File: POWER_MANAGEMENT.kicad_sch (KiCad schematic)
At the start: 13 parts, among them J5 LIPO PIN

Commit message: Revision
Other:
- moved on the sheet: NCD0603G1, R7
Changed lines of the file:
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@@
+	(wire
+		(pts
+			(xy 40.64 81.28) (xy 40.64 85.09)
+		)
+		(stroke
+			(width 0)
+			(type default)
+		)
+	)
 	(wire
 		(pts
@@
 	(wire
 		(pts
-			(xy 49.53 93.98) (xy 49.53 101.6)
+			(xy 40.64 90.17) (xy 40.64 97.79)
 		)
 		(stroke
@@
 	(wire
 		(pts
-			(xy 49.53 116.84) (xy 49.53 109.22)
+			(xy 40.64 114.3) (xy 40.64 105.41)
 		)
 		(stroke
@@
 	(hierarchical_label "LED"
 		(shape input)
-		(at 49.53 88.9 90)
+		(at 40.64 81.28 90)
 		(effects
 			(font
@@
 	(symbol
 		(lib_id "Device:R_Small")
-		(at 49.53 91.44 0)
+		(at 40.64 87.63 0)
 		(unit 1)
 		(exclude_from_sim no)
@@
 		(dnp no)
 		(property "Reference" "R7"
-			(at 54.61 91.44 0)
+			(at 45.72 87.63 0)
 			(effects
 				(font
@@
 		)
 		(property "Value" "5.4k"
-			(at 55.372 87.884 0)
+			(at 46.482 84.074 0)
 			(effects
 				(font
@@
 		)
 		(property "Footprint" "Resistor_SMD:R_0402_1005Metric"
-			(at 49.53 91.44 0)
+			(at 40.64 87.63 0)
 			(effects
 				(font
@@
 		)
 		(property "Datasheet" "~"
-			(at 49.53 91.44 0)
+			(at 40.64 87.63 0)
 			(effects
 				(font
@@
 		)
 		(property "Description" "Resistor, small symbol"
-			(at 49.53 91.44 0)
+			(at 40.64 87.63 0)
 			(effects
 				(font
@@
 		)
 		(property "SNAPEDA_PN" ""
-			(at 49.53 91.44 0)
+			(at 40.64 87.63 0)
 			(effects
 				(font
@@
 		(dnp no)
 		(property "Reference" "NCD0603R1"
-			(at 73.9775 102.87 90)
+			(at 75.946 101.854 90)
 			(effects
 				(font
@@
 		)
 		(property "Value" "RED_LED"
-			(at 73.9775 105.41 90)
+			(at 75.946 104.394 90)
 			(effects
 				(font
@@
 	(symbol
 		(lib_id "power:GND")
-		(at 49.53 116.84 0)
+		(at 40.64 114.3 0)
 		(unit 1)
 		(exclude_from_sim no)
@@
 		(dnp no)
 		(property "Reference" "#PWR035"
-			(at 49.53 123.19 0)
+			(at 40.64 120.65 0)
 			(effects
 				(font
@@
 		)
 		(property "Value" "GND"
-			(at 56.134 120.142 0)
+			(at 47.244 117.602 0)
 			(effects
 				(font
@@
 		)
 		(property "Footprint" ""
-			(at 49.53 116.84 0)
+			(at 40.64 114.3 0)
 			(effects
 				(font
@@
 		)
 		(property "Datasheet" ""
-			(at 49.53 116.84 0)
+			(at 40.64 114.3 0)
 			(effects
 				(font
@@
 		)
 		(property "Description" "Power symbol creates a global label with name \"GND\" , ground"
-			(at 49.53 116.84 0)
+			(at 40.64 114.3 0)
 			(effects
 				(font
@@
 	(symbol
 		(lib_id "Device:LED")
-		(at 49.53 105.41 90)
+		(at 40.64 101.6 90)
 		(unit 1)
 		(exclude_from_sim no)
@@
 		(dnp no)
 		(property "Reference" "NCD0603G1"
-			(at 56.1975 105.41 90)
+			(at 49.784 99.822 90)
 			(effects
 				(font
@@
 		)
 		(property "Value" "GREEN LED"
-			(at 56.1975 107.95 90)
+			(at 49.784 102.362 90)
 			(effects
 				(font
@@
 		)
 		(property "Footprint" "LED_SMD:LED_0603_1608Metric"
-			(at 49.53 105.41 0)
+			(at 40.64 101.6 0)
 			(effects
 				(font
@@
 		)
 		(property "Datasheet" "~"
-			(at 49.53 105.41 0)
+			(at 40.64 101.6 0)
 			(effects
 				(font
@@
 		)
 		(property "Description" "Light emitting diode"
-			(at 49.53 105.41 0)
+			(at 40.64 101.6 0)
 			(effects
 				(font
@@
 		)
 		(property "Sim.Pins" "1=K 2=A"
-			(at 49.53 105.41 0)
+			(at 40.64 101.6 0)
 			(effects
 				(font
@@
 		)
 		(property "SNAPEDA_PN" ""
-			(at 49.53 105.41 90)
-			(effects
-				(font
+			(at 40.64 101.6 90)
+			(effects
+				(font

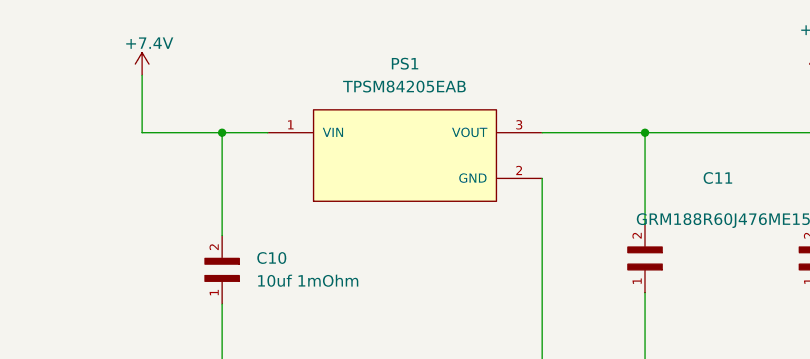
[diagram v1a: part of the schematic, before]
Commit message: update Schematic
Fixed N channel mosfet pyros and set to low side trigger
removed unneeded 5v buck converter
rerouted/optmized gpio pins
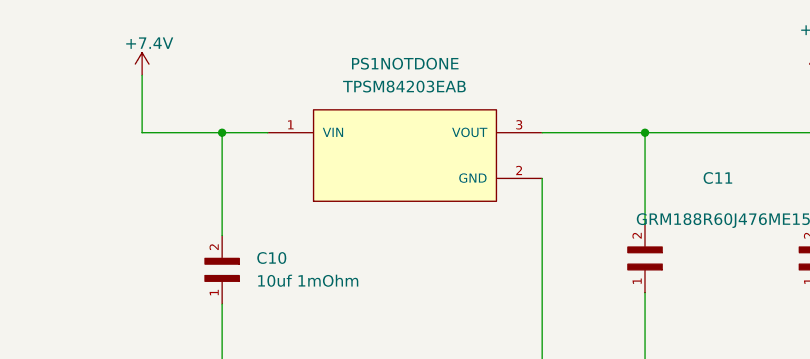
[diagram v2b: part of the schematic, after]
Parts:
- PS1NOTDONE: renamed from PS1; value TPSM84205EAB -> TPSM84203EAB
- renumbered C13 to C12
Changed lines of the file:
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@@
 		(instances
 			(project "Experimental"
-				(path "/d685641e-0e6b-462c-92c0-fbf0ccf1a433/a795adf3-e3bc-45dd-be3f-b4f420161d74"
+				(path "/d685641e-0e6b-462c-92c0-fbf0ccf1a433/8d3a2210-5160-49c4-9bac-feecf85a4c4a"
 					(reference "C1")
 					(unit 1)
@@
 		(on_board yes)
 		(dnp no)
-		(property "Reference" "#PWR016"
+		(property "Reference" "#PWR014"
 			(at 67.31 83.82 0)
 			(effects
@@
 		(instances
 			(project "Experimental"
-				(path "/d685641e-0e6b-462c-92c0-fbf0ccf1a433/a795adf3-e3bc-45dd-be3f-b4f420161d74"
-					(reference "#PWR016")
+				(path "/d685641e-0e6b-462c-92c0-fbf0ccf1a433/8d3a2210-5160-49c4-9bac-feecf85a4c4a"
+					(reference "#PWR014")
 					(unit 1)
 				)
@@
 		(on_board yes)
 		(dnp no)
-		(property "Reference" "#PWR055"
+		(property "Reference" "#PWR028"
 			(at 121.92 160.02 0)
 			(effects
@@
 		(instances
 			(project "Experimental"
-				(path "/d685641e-0e6b-462c-92c0-fbf0ccf1a433/a795adf3-e3bc-45dd-be3f-b4f420161d74"
-					(reference "#PWR055")
+				(path "/d685641e-0e6b-462c-92c0-fbf0ccf1a433/8d3a2210-5160-49c4-9bac-feecf85a4c4a"
+					(reference "#PWR028")
 					(unit 1)
 				)
@@
 		(on_board yes)
 		(dnp no)
-		(property "Reference" "C13"
+		(property "Reference" "C12"
 			(at 230.886 76.708 90)
 			(effects
@@
 		(instances
 			(project "Experimental"
-				(path "/d685641e-0e6b-462c-92c0-fbf0ccf1a433/a795adf3-e3bc-45dd-be3f-b4f420161d74"
-					(reference "C13")
+				(path "/d685641e-0e6b-462c-92c0-fbf0ccf1a433/8d3a2210-5160-49c4-9bac-feecf85a4c4a"
+					(reference "C12")
 					(unit 1)
 				)
@@
 		(instances
 			(project "Experimental"
-				(path "/d685641e-0e6b-462c-92c0-fbf0ccf1a433/a795adf3-e3bc-45dd-be3f-b4f420161d74"
+				(path "/d685641e-0e6b-462c-92c0-fbf0ccf1a433/8d3a2210-5160-49c4-9bac-feecf85a4c4a"
 					(reference "R7")
 					(unit 1)
@@
 		(instances
 			(project "Experimental"
-				(path "/d685641e-0e6b-462c-92c0-fbf0ccf1a433/a795adf3-e3bc-45dd-be3f-b4f420161d74"
+				(path "/d685641e-0e6b-462c-92c0-fbf0ccf1a433/8d3a2210-5160-49c4-9bac-feecf85a4c4a"
 					(reference "C10")
 					(unit 1)
@@
 		(instances
 			(project "Experimental"
-				(path "/d685641e-0e6b-462c-92c0-fbf0ccf1a433/a795adf3-e3bc-45dd-be3f-b4f420161d74"
+				(path "/d685641e-0e6b-462c-92c0-fbf0ccf1a433/8d3a2210-5160-49c4-9bac-feecf85a4c4a"
 					(reference "C2")
 					(unit 1)
@@
 		(on_board yes)
 		(dnp no)
-		(property "Reference" "#PWR017"
+		(property "Reference" "#PWR015"
 			(at 67.31 120.65 0)
 			(effects
@@
 		(instances
 			(project "Experimental"
-				(path "/d685641e-0e6b-462c-92c0-fbf0ccf1a433/a795adf3-e3bc-45dd-be3f-b4f420161d74"
-					(reference "#PWR017")
+				(path "/d685641e-0e6b-462c-92c0-fbf0ccf1a433/8d3a2210-5160-49c4-9bac-feecf85a4c4a"
+					(reference "#PWR015")
 					(unit 1)
 				)
@@
 		(dnp no)
 		(fields_autoplaced yes)
-		(property "Reference" "#PWR015"
+		(property "Reference" "#PWR026"
 			(at 105.41 118.11 0)
 			(effects
@@
 		(instances
 			(project "Experimental"
-				(path "/d685641e-0e6b-462c-92c0-fbf0ccf1a433/a795adf3-e3bc-45dd-be3f-b4f420161d74"
-					(reference "#PWR015")
+				(path "/d685641e-0e6b-462c-92c0-fbf0ccf1a433/8d3a2210-5160-49c4-9bac-feecf85a4c4a"
+					(reference "#PWR026")
 					(unit 1)
 				)
@@
 		(dnp no)
 		(fields_autoplaced yes)
-		(property "Reference" "#PWR013"
+		(property "Reference" "#PWR016"
 			(at 93.98 87.63 0)
 			(effects
@@
 		(instances
 			(project "Experimental"
-				(path "/d685641e-0e6b-462c-92c0-fbf0ccf1a433/a795adf3-e3bc-45dd-be3f-b4f420161d74"
-					(reference "#PWR013")
+				(path "/d685641e-0e6b-462c-92c0-fbf0ccf1a433/8d3a2210-5160-49c4-9bac-feecf85a4c4a"
+					(reference "#PWR016")
 					(unit 1)
 				)
@@
 		(on_board yes)
 		(dnp no)
-		(property "Reference" "#PWR028"
+		(property "Reference" "#PWR017"
 			(at 93.98 139.7 0)
 			(effects
@@
 		(instances
 			(project "Experimental"
-				(path "/d685641e-0e6b-462c-92c0-fbf0ccf1a433/a795adf3-e3bc-45dd-be3f-b4f420161d74"
-					(reference "#PWR028")
+				(path "/d685641e-0e6b-462c-92c0-fbf0ccf1a433/8d3a2210-5160-49c4-9bac-feecf85a4c4a"
+					(reference "#PWR017")
 					(unit 1)
 				)
@@
 		(on_board yes)
 		(dnp no)
-		(property "Reference" "#PWR026"
+		(property "Reference" "#PWR035"
 			(at 191.77 123.19 0)
 			(effects
@@
 		(instances
 			(project "Experimental"
-				(path "/d685641e-0e6b-462c-92c0-fbf0ccf1a433/a795adf3-e3bc-45dd-be3f-b4f420161d74"
-					(reference "#PWR026")
+				(path "/d685641e-0e6b-462c-92c0-fbf0ccf1a433/8d3a2210-5160-49c4-9bac-feecf85a4c4a"
+					(reference "#PWR035")
 					(unit 1)
 				)
@@
 		(instances
 			(project "Experimental"
-				(path "/d685641e-0e6b-462c-92c0-fbf0ccf1a433/a795adf3-e3bc-45dd-be3f-b4f420161d74"
+				(path "/d685641e-0e6b-462c-92c0-fbf0ccf1a433/8d3a2210-5160-49c4-9bac-feecf85a4c4a"
 					(reference "5v1")
 					(unit 1)
@@
 		(instances
 			(project "Experimental"
-				(path "/d685641e-0e6b-462c-92c0-fbf0ccf1a433/a795adf3-e3bc-45dd-be3f-b4f420161d74"
+				(path "/d685641e-0e6b-462c-92c0-fbf0ccf1a433/8d3a2210-5160-49c4-9bac-feecf85a4c4a"
 					(reference "NCD0603R1")
 					(unit 1)
@@
 		(on_board yes)
 		(dnp no)
-		(property "Reference" "#PWR029"
+		(property "Reference" "#PWR025"
 			(at 93.98 160.02 0)
 			(effects
@@
 		(instances
 			(project "Experimental"
-				(path "/d685641e-0e6b-462c-92c0-fbf0ccf1a433/a795adf3-e3bc-45dd-be3f-b4f420161d74"
-					(reference "#PWR029")
+				(path "/d685641e-0e6b-462c-92c0-fbf0ccf1a433/8d3a2210-5160-49c4-9bac-feecf85a4c4a"
+					(reference "#PWR025")
 					(unit 1)
 				)
@@
 		(dnp no)
 		(fields_autoplaced yes)
-		(property "Reference" "PS1"
+		(property "Reference" "PS1NOTDONE"
 			(at 176.53 74.93 0)
 			(effects
@@
 			)
 		)
-		(property "Value" "TPSM84205EAB"
+		(property "Value" "TPSM84203EAB"
 			(at 176.53 77.47 0)
 			(effects
@@
 		)
 		(instances
-			(project ""
-				(path "/d685641e-0e6b-462c-92c0-fbf0ccf1a433/a795adf3-e3bc-45dd-be3f-b4f420161d74"
-					(reference "PS1")
+			(project "Experimental"
+				(path "/d685641e-0e6b-462c-92c0-fbf0ccf1a433/8d3a2210-5160-49c4-9bac-feecf85a4c4a"
+					(reference "PS1NOTDONE")
 					(unit 1)
 				)
@@
 		(on_board yes)
 		(dnp no)
-		(property "Reference" "#PWR035"
+		(property "Reference" "#PWR013"
 			(at 40.64 120.65 0)
 			(effects
@@
 		(instances
 			(project "Experimental"
-				(path "/d685641e-0e6b-462c-92c0-fbf0ccf1a433/a795adf3-e3bc-45dd-be3f-b4f420161d74"
-					(reference "#PWR035")
+				(path "/d685641e-0e6b-462c-92c0-fbf0ccf1a433/8d3a2210-5160-49c4-9bac-feecf85a4c4a"
+					(reference "#PWR013")
 					(unit 1)
 				)
@@
 		)
 		(instances
-			(project ""
-				(path "/d685641e-0e6b-462c-92c0-fbf0ccf1a433/a795adf3-e3bc-45dd-be3f-b4f420161d74"
+			(project "Experimental"
+				(path "/d685641e-0e6b-462c-92c0-fbf0ccf1a433/8d3a2210-5160-49c4-9bac-feecf85a4c4a"
 					(reference "J5")
 					(unit 1)
@@
 		(instances
 			(project "Experimental"
-				(path "/d685641e-0e6b-462c-92c0-fbf0ccf1a433/a795adf3-e3bc-45dd-be3f-b4f420161d74"
+				(path "/d685641e-0e6b-462c-92c0-fbf0ccf1a433/8d3a2210-5160-49c4-9bac-feecf85a4c4a"
 					(reference "D1")
 					(unit 1)
@@
 		(dnp no)
 		(fields_autoplaced yes)
-		(property "Reference" "#PWR027"
+		(property "Reference" "#PWR050"
 			(at 222.25 80.01 0)
 			(effects
@@
 		(instances
 			(project "Experimental"
-				(path "/d685641e-0e6b-462c-92c0-fbf0ccf1a433/a795adf3-e3bc-45dd-be3f-b4f420161d74"
-					(reference "#PWR027")
+				(path "/d685641e-0e6b-462c-92c0-fbf0ccf1a433/8d3a2210-5160-49c4-9bac-feecf85a4c4a"
+					(reference "#PWR050")
 					(unit 1)
 				)
@@
 		(instances
 			(project "Experimental"
-				(path "/d685641e-0e6b-462c-92c0-fbf0ccf1a433/a795adf3-e3bc-45dd-be3f-b4f420161d74"
+				(path "/d685641e-0e6b-462c-92c0-fbf0ccf1a433/8d3a2210-5160-49c4-9bac-feecf85a4c4a"
 					(reference "R8")
 					(unit 1)
@@
 		(on_board yes)
 		(dnp no)
-		(property "Reference" "#PWR025"
+		(property "Reference" "#PWR029"
 			(at 147.32 80.01 0)
 			(effects
@@
 		(instances
 			(project "Experimental"
-				(path "/d685641e-0e6b-462c-92c0-fbf0ccf1a433/a795adf3-e3bc-45dd-be3f-b4f420161d74"
-					(reference "#PWR025")
+				(path "/d685641e-0e6b-462c-92c0-fbf0ccf1a433/8d3a2210-5160-49c4-9bac-feecf85a4c4a"
+					(reference "#PWR029")
 					(unit 1)
 				)
@@
 		(instances
 			(project "Experimental"
-				(path "/d685641e-0e6b-462c-92c0-fbf0ccf1a433/a795adf3-e3bc-45dd-be3f-b4f420161d74"
+				(path "/d685641e-0e6b-462c-92c0-fbf0ccf1a433/8d3a2210-5160-49c4-9bac-feecf85a4c4a"
 					(reference "C11")
 					(unit 1)
@@
 		(instances
 			(project "Experimental"
-				(path "/d685641e-0e6b-462c-92c0-fbf0ccf1a433/a795adf3-e3bc-45dd-be3f-b4f420161d74"
+				(path "/d685641e-0e6b-462c-92c0-fbf0ccf1a433/8d3a2210-5160-49c4-9bac-feecf85a4c4a"
 					(reference "NCD0603G1")
 					(unit 1)
@@
 		(dnp no)
 		(fields_autoplaced yes)
-		(property "Reference" "#PWR014"
+		(property "Reference" "#PWR027"
 			(at 115.57 87.63 0)
 			(effects
@@
 		(instances
 			(project "Experimental"
-				(path "/d685641e-0e6b-462c-92c0-fbf0ccf1a433/a795adf3-e3bc-45dd-be3f-b4f420161d74"
-					(reference "#PWR014")
-					(unit 1)
-				)
+				(path "/d685641e-0e6b-462c-92c0-fbf0ccf1a433/8d3a2210-5160-49c4-9bac-feecf85a4c4a"
+					(reference "#PWR027")
+					(unit 1)
+				)

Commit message: Tweaks and readability
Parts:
- 5v1: value LP5907MFX-3.3/NOPB -> LP5907MFX-3.3
- C11: value GRM188R60J476ME15D -> 47uF 3.037mOhm
- C13: renamed from C12; value GRM188R60J476ME15D -> 06034W476MAT2A
- PS1: renamed from PS1NOTDONE; value TPSM84203EAB -> TPSM84205EAB
- renumbered NCD0603G1 to BLINKY1, NCD0603R1 to OnLight1
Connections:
- net +7.4V: now also D1.2 (A2); no longer D1.1 (A1)
- net GND: now also D1.1 (A1); no longer D1.2 (A2)
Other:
- moved on the sheet: BLINKY1, D1, R7
